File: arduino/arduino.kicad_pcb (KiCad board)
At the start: 2 copper layers, 12 parts, among them IC1 ATMEGA328P-P, P1 CONN_6, P2 CONN_2, P3 CONN_6, P4 CONN_6, P5 CONN_1, U1 RFM12B

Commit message: first valid layout - added connector
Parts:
- added P6: CONN_6, PINHEAD1-6, F.Cu at (113.5, 120.9)
- added Q1: 16MHz, murata-resonators-CSTLS_G8, F.Cu at (108.3, 125.1)
- C2, C4: value C -> 0.1u
- C3: value CP1 -> 10u
- R1: value R -> 10k
- moved C1 24.6 mm to (93.5, 132.5), turned to 270 degrees
- moved C4 11.2 mm to (107.1, 143.8), turned to 90 degrees
- moved P5 8.02 mm to (92.5, 112.4)
- moved P1 0.77 mm to (112.0, 144.5)
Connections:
- IC1 pad 12: (no net) -> N-0000013
- IC1 pad 13: (no net) -> N-0000011
- IC1 pad 14: (no net) -> N-0000014
- IC1 pad 16: (no net) -> N-0000015
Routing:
- net GND: track 43.1 -> 117.1 mm, vias 1 -> 0
- net N-0000029: track 0.00 -> 52.4 mm, vias 0 -> 3
- net N-0000026: track 0.00 -> 26.5 mm, vias 0 -> 1
- net VCC: track 97.4 -> 118.8 mm
- net N-0000015: track 0.00 -> 19.7 mm
- net N-000009: track 0.00 -> 17.5 mm
- net N-0000014: track 0.00 -> 10.2 mm
- net N-0000013: track 0.00 -> 10.1 mm
- net N-0000011: track 0.00 -> 10.0 mm
- net N-0000036: track 0.00 -> 6.85 mm
- net N-000008: track 0.00 -> 6.45 mm
- net N-000004: track 0.00 -> 5.68 mm
- net N-000003: track 0.00 -> 4.66 mm
- net N-0000031: track 0.00 -> 3.46 mm
- net N-0000022: track 9.41 -> 11.1 mm
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
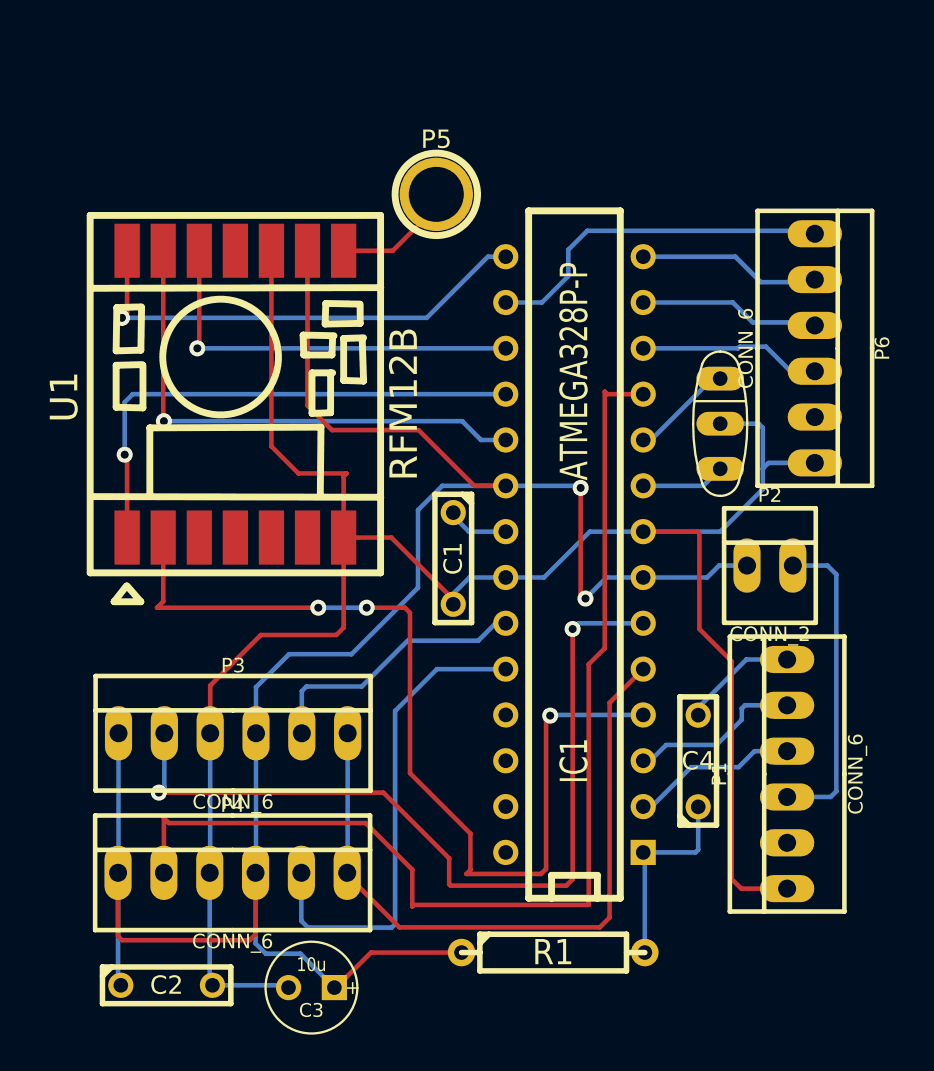
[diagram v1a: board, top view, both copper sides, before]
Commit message: change connectors
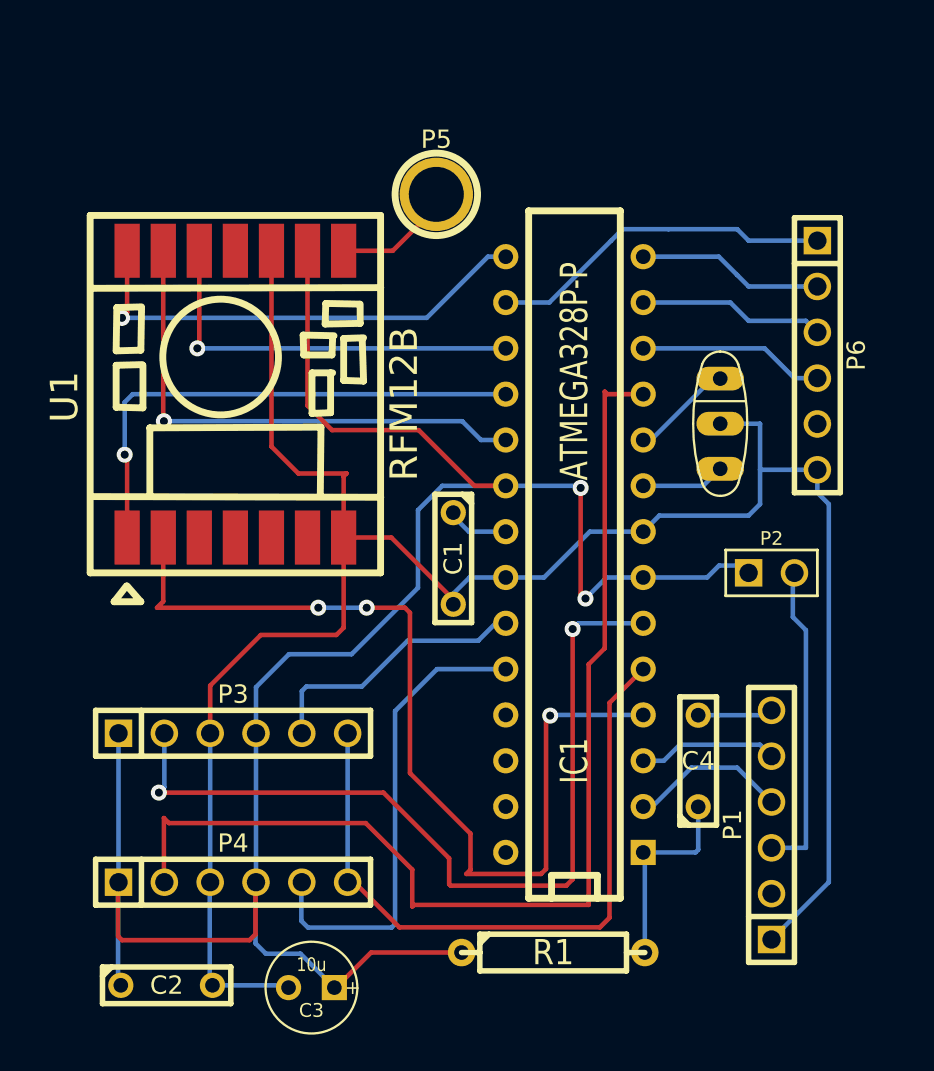
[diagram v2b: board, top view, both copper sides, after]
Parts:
- P1, P3, P4, P6: footprint PINHEAD1-6 -> PIN_ARRAY-6X1
- P2: footprint PINHEAD1-2 -> PIN_ARRAY_2X1
- moved P1 2.95 mm to (111.1, 147.3)
- moved P4 0.52 mm to (81.3, 150.5)
- moved P2 0.42 mm to (111.1, 133.3)
- moved P6 0.41 mm to (113.7, 121.3)
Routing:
- net N-000008: track 6.45 -> 4.17 mm
- net N-000007: track 9.61 -> 7.74 mm
- net GND: track 117.1 -> 118.8 mm

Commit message: more pcb work
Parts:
- P5: footprint 1pin -> PIN_ARRAY_1
- moved P1 3.81 mm to (111.1, 143.5)
- moved R1 2.74 mm to (97.8, 156.8)
- moved P2 2.01 mm to (109.2, 132.7)
- moved P5 1.94 mm to (92.7, 114.3)
- moved IC1 0.64 mm to (99.7, 132.7)
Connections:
- P6 pad 5: (no net) -> VCC
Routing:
- net VCC: track 118.8 -> 128.1 mm
- net N-000008: track 4.17 -> 7.99 mm
- net GND: track 118.8 -> 115.0 mm
- net N-0000021: track 11.1 -> 14.1 mm
- net N-0000012: track 38.4 -> 41.2 mm
- net N-000009: track 7.74 -> 9.91 mm
- net N-000007: track 47.4 -> 48.9 mm, vias 2 -> 1
- net N-000006: track 17.9 -> 16.5 mm
- net N-0000010: track 60.9 -> 59.5 mm
- net N-0000035: track 6.85 -> 5.80 mm
- net N-0000027: track 52.4 -> 51.4 mm
- added copper zone on B.Cu, net (none)
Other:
- board outline added: 45.1 x 47.6 mm

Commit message: remove ground plane temporarily
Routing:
- removed copper zone on B.Cu, net (none)
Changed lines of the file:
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@@
   (segment (start 74.93 142.24) (end 74.93 149.9489) (width 0.254) (layer B.Cu) (net 25))
   (segment (start 74.93 149.9489) (end 74.9046 149.9743) (width 0.254) (layer B.Cu) (net 25))
-  (zone (net 0) (net_name "") (layer B.Cu) (hatch edge 0.508)
-    (connect_pads (clearance 0.508))
-    (min_thickness 0.254)
-    (fill (arc_segments 16) (thermal_gap 0.508) (thermal_bridge_width 0.508))
-    (polygon
-      (pts
-        (xy 116.205 158.115) (xy 72.39 158.115) (xy 72.39 111.76) (xy 116.205 111.76)
-      )
-    )
-  )
 )

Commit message: wip : moving parts about
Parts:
- moved R1 16.4 mm to (107.3, 143.5), turned to 270 degrees
- moved C4 9.27 mm to (106.7, 153.0), turned to 0 degrees
- moved C2 6.99 mm to (77.5, 149.2)
- moved C3 6.58 mm to (84.5, 149.9)
- moved P4 5.72 mm to (81.3, 144.8)
- moved P3 2.54 mm to (81.3, 139.7)
- moved Q1 1.73 mm to (106.7, 125.7)
- moved P1 0.90 mm to (110.5, 142.9), turned to 270 degrees
- moved P2 0.90 mm to (108.6, 132.1)
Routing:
- net GND: track 115.0 -> 94.3 mm, vias 0 -> 1
- net VCC: track 128.1 -> 140.8 mm, vias 2 -> 0
- net N-0000010: track 59.5 -> 67.3 mm
- net N-0000011: track 27.0 -> 20.3 mm
- net N-0000021: track 14.1 -> 8.15 mm
- net N-000007: track 48.9 -> 54.6 mm
- net N-000006: track 16.5 -> 11.2 mm
- net N-0000027: track 51.4 -> 55.3 mm, vias 3 -> 1
- net N-000008: track 7.99 -> 4.34 mm
- net N-0000012: track 41.2 -> 43.3 mm, vias 0 -> 1
- net N-000009: track 9.91 -> 8.04 mm, vias 0 -> 1
- net N-000005: track 15.2 -> 14.0 mm
- net N-000003: track 4.66 -> 3.45 mm
- net N-000004: track 5.68 -> 4.47 mm
- net N-0000033: track 8.80 -> 8.04 mm

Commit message: wip
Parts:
- moved R1 0.63 mm to (106.7, 143.5), turned to 90 degrees
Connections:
- C4 pad 1: N-0000021 (its old number) -> N-0000016
- IC1 pad 1: N-0000021 (its old number) -> N-0000016
- R1 pad 1: VCC -> N-0000016
- R1 pad 2: N-0000021 (its old number) -> VCC
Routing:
- net N-0000021 (its old number): track 8.15 -> 0.00 mm
- net N-0000016: track 0.00 -> 7.51 mm

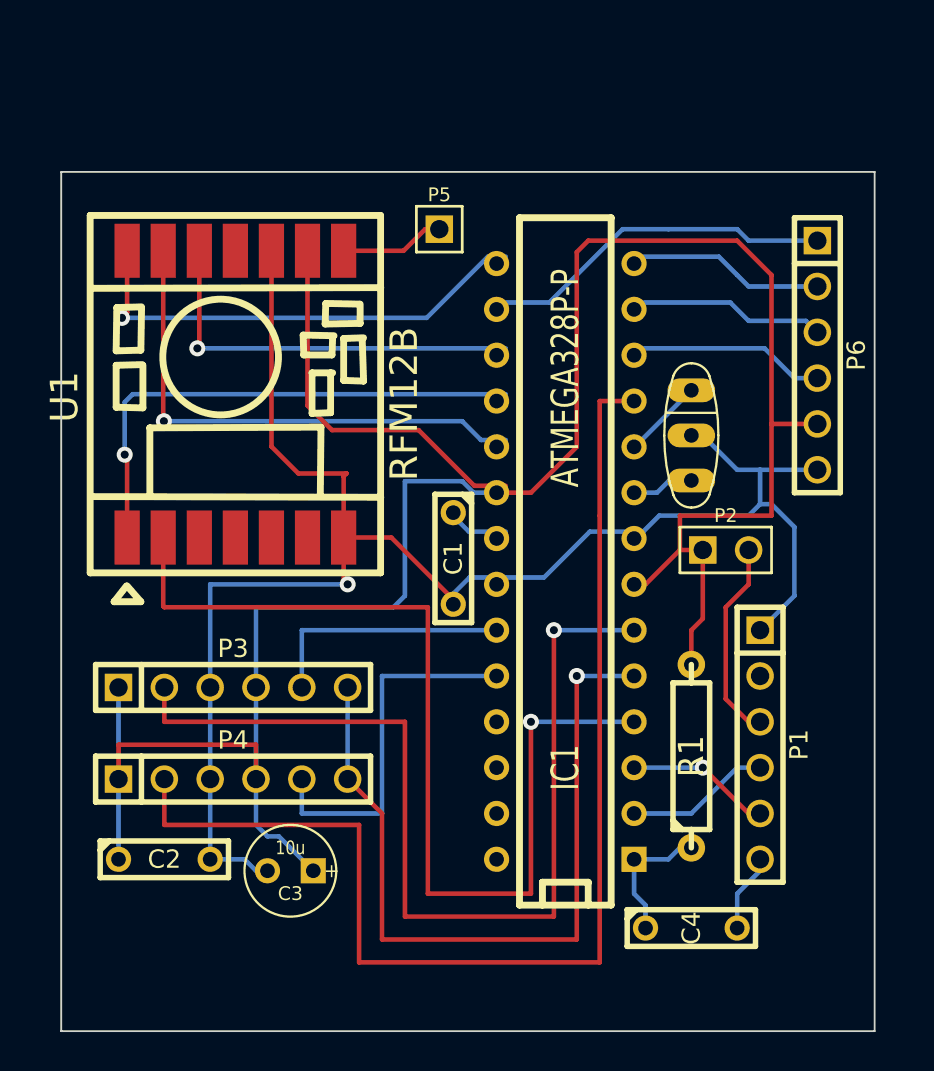
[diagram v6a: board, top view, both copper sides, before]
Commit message: moving traces slightly
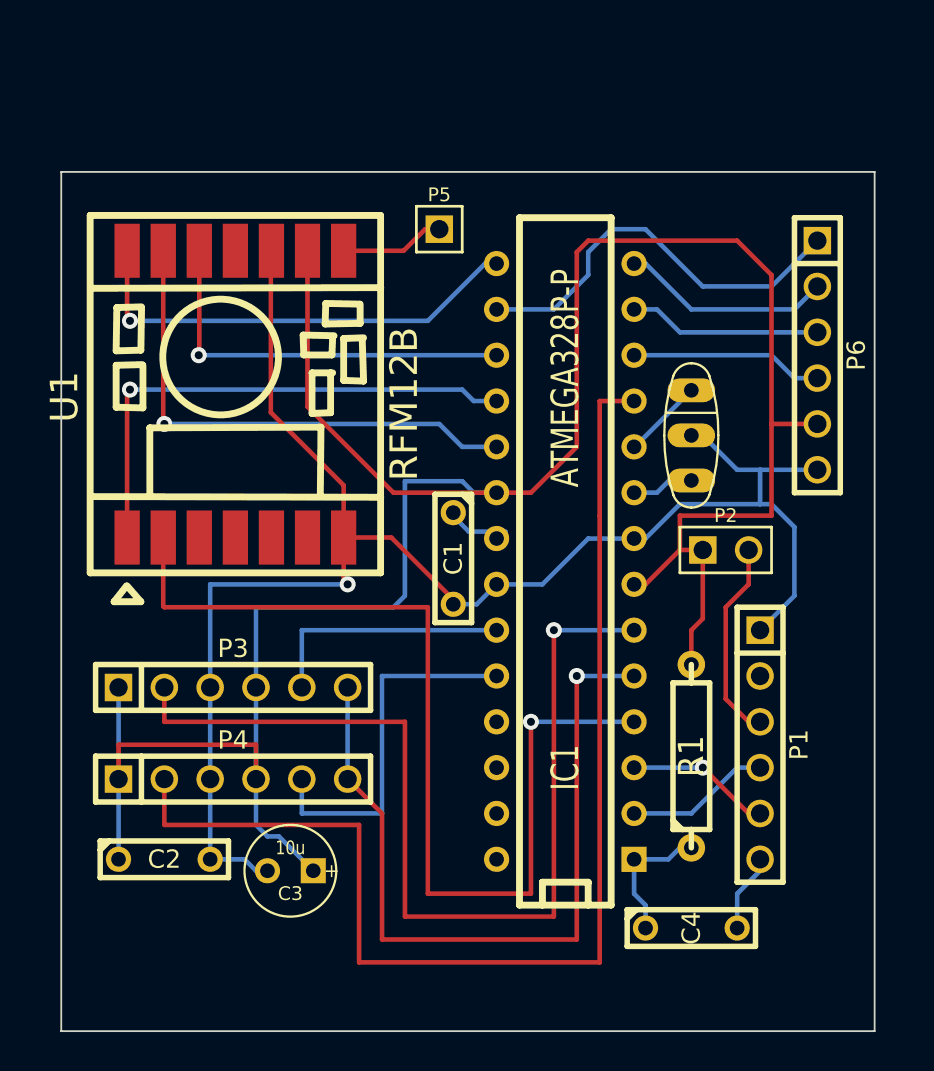
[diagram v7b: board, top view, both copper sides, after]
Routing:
- net N-0000013: track 19.2 -> 22.7 mm
- net GND: track 94.3 -> 92.2 mm
- net N-0000014: track 10.3 -> 11.7 mm
- net N-0000021: track 26.5 -> 25.6 mm

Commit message: shrink board, add mounting holes
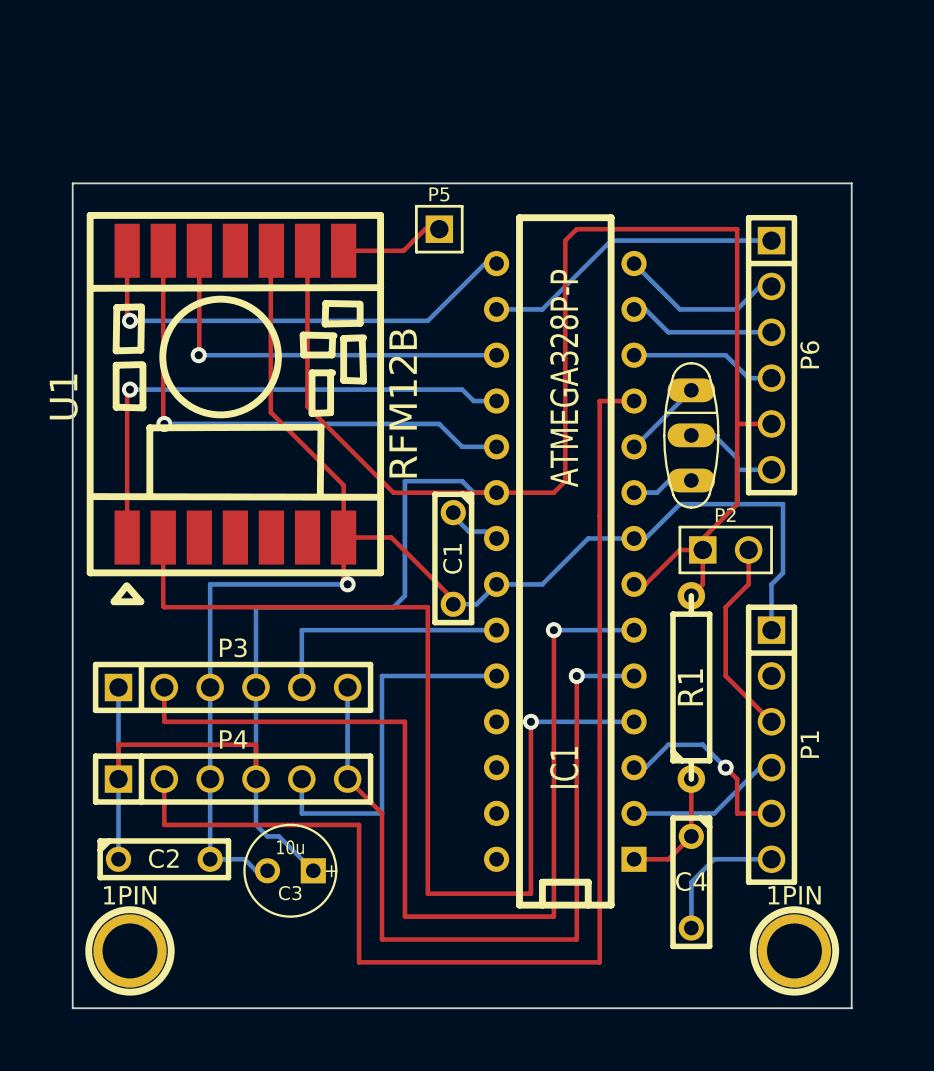
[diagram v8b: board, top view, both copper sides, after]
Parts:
- added 1PIN: P***, 1pin, F.Cu at (75.6, 154.3)
- added 1PIN: P***, 1pin, F.Cu at (112.4, 154.3)
- moved R1 3.81 mm to (106.7, 139.7)
- moved P6 2.54 mm to (111.1, 121.3)
- moved C4 2.54 mm to (106.7, 150.5), turned to 270 degrees
- moved P1 0.64 mm to (111.1, 142.9)
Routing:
- net VCC: track 140.8 -> 133.6 mm
- net N-0000013: track 22.7 -> 16.8 mm
- net N-000009: track 4.34 -> 7.51 mm
- net N-0000034: track 8.04 -> 10.8 mm
- net GND: track 92.2 -> 89.7 mm
- net N-0000015: track 10.7 -> 8.15 mm
- net N-0000012: track 10.7 -> 8.15 mm
- net N-0000014: track 11.7 -> 9.20 mm
- net N-0000035: track 8.04 -> 8.67 mm
- net N-0000016: track 7.51 -> 6.88 mm
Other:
- board size 45.1 x 47.6 mm -> 43.2 x 45.7 mm
